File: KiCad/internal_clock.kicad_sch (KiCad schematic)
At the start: 8 parts, among them U1 TL074

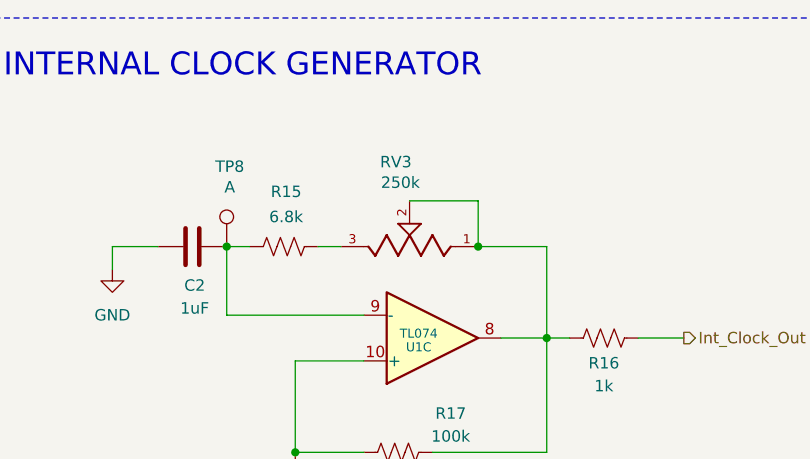
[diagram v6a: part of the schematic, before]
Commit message: re-placing components; optimizing text on silkscreen
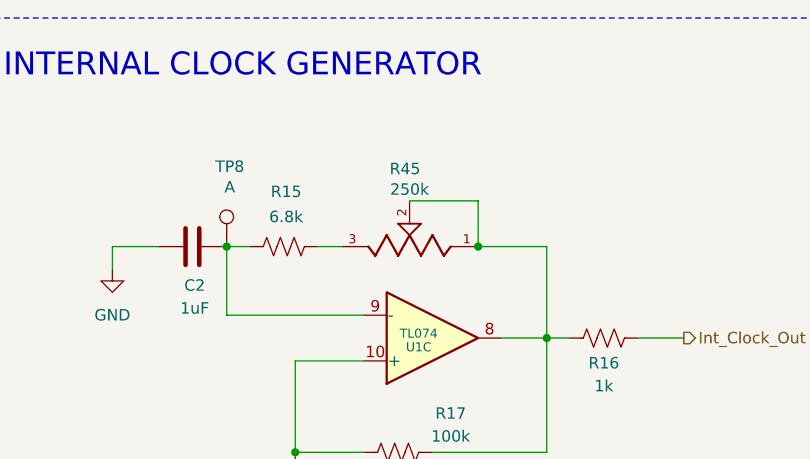
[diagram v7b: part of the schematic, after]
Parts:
- removed RV3: 250k, Eurorack:RD901F_1, symbol Eurorack:RD901F
- added R45: 250k, Eurorack:Potentiometer_Alpha_RD901F_Vertical_Alt, symbol Eurorack:Potentiometer_Alpha_RD901F_Vertical
- C2: footprint Eurorack:Kemet Film Cap -> Eurorack:Capacitor_Film_KEMET_R82DC4100AA60J_THT
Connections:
- net at R16.2, R17.1, U1.8: now also R45.1, R45.2
- net at R15.1: now also R45.3
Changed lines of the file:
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@@
-	)
-	(symbol
-		(lib_id "Eurorack:RD901F")
-		(at 68.58 45.72 180)
-		(unit 1)
-		(exclude_from_sim no)
-		(in_bom yes)
-		(on_board yes)
-		(dnp no)
-		(property "Reference" "RV3"
-			(at 67.056 36.322 0)
-			(effects
-				(font
-					(size 1.27 1.27)
-				)
-			)
-		)
-		(property "Value" "250k"
-			(at 67.564 38.608 0)
-			(effects
-				(font
-					(size 1.27 1.27)
-				)
-			)
-		)
-		(property "Footprint" "Eurorack:RD901F_1"
-			(at 68.58 45.72 0)
-			(effects
-				(font
-					(size 1.27 1.27)
-				)
-				(justify bottom)
-				(hide yes)
-			)
-		)
-		(property "Datasheet" ""
-			(at 68.58 45.72 0)
-			(effects
-				(font
-					(size 1.27 1.27)
-				)
-				(hide yes)
-			)
-		)
-		(property "Description" ""
-			(at 68.58 45.72 0)
-			(effects
-				(font
-					(size 1.27 1.27)
-				)
-				(hide yes)
-			)
-		)
-		(property "MF" ""
-			(at 68.58 45.72 0)
-			(effects
-				(font
-					(size 1.27 1.27)
-				)
-				(justify bottom)
-				(hide yes)
-			)
-		)
-		(property "MAXIMUM_PACKAGE_HEIGHT" ""
-			(at 68.58 45.72 0)
-			(effects
-				(font
-					(size 1.27 1.27)
-				)
-				(justify bottom)
-				(hide yes)
-			)
-		)
-		(property "Package" ""
-			(at 68.58 45.72 0)
-			(effects
-				(font
-					(size 1.27 1.27)
-				)
-				(justify bottom)
-				(hide yes)
-			)
-		)
-		(property "Price" ""
-			(at 68.58 45.72 0)
-			(effects
-				(font
-					(size 1.27 1.27)
-				)
-				(justify bottom)
-				(hide yes)
-			)
-		)
-		(property "Check_prices" ""
-			(at 68.58 45.72 0)
-			(effects
-				(font
-					(size 1.27 1.27)
-				)
-				(justify bottom)
-				(hide yes)
-			)
-		)
-		(property "STANDARD" ""
-			(at 68.58 45.72 0)
-			(effects
-				(font
-					(size 1.27 1.27)
-				)
-				(justify bottom)
-				(hide yes)
-			)
-		)
-		(property "PARTREV" ""
-			(at 68.58 45.72 0)
-			(effects
-				(font
-					(size 1.27 1.27)
-				)
-				(justify bottom)
-				(hide yes)
-			)
-		)
-		(property "SnapEDA_Link" ""
-			(at 68.58 45.72 0)
-			(effects
-				(font
-					(size 1.27 1.27)
-				)
-				(justify bottom)
-				(hide yes)
-			)
-		)
-		(property "MP" ""
-			(at 68.58 45.72 0)
-			(effects
-				(font
-					(size 1.27 1.27)
-				)
-				(justify bottom)
-				(hide yes)
-			)
-		)
-		(property "Description_1" ""
-			(at 68.58 45.72 0)
-			(effects
-				(font
-					(size 1.27 1.27)
-				)
-				(justify bottom)
-				(hide yes)
-			)
-		)
-		(property "Availability" ""
-			(at 68.58 45.72 0)
-			(effects
-				(font
-					(size 1.27 1.27)
-				)
-				(justify bottom)
-				(hide yes)
-			)
-		)
-		(property "MANUFACTURER" ""
-			(at 68.58 45.72 0)
-			(effects
-				(font
-					(size 1.27 1.27)
-				)
-				(justify bottom)
-				(hide yes)
-			)
-		)
-		(pin "1"
-		)
-		(pin "2"
-		)
-		(pin "3"
-		)
-		(instances
-			(project ""
-				(path "/c997e785-a132-463f-bd08-a5a67a697207/b964167f-08d9-430a-9aa0-9a2613885304"
-					(reference "RV3")
-					(unit 1)
-				)
-			)
-		)
 	)
 	(symbol
@@
 			)
 		)
-		(property "Footprint" "Eurorack:Kemet Film Cap"
+		(property "Footprint" "Eurorack:Capacitor_Film_KEMET_R82DC4100AA60J_THT"
 			(at 48.26 44.7548 0)
 			(effects
@@
 					(unit 1)
 				)
+			)
+		)
+	)
+	(symbol
+		(lib_id "Eurorack:Potentiometer_Alpha_RD901F_Vertical")
+		(at 68.58 45.72 180)
+		(unit 1)
+		(exclude_from_sim no)
+		(in_bom yes)
+		(on_board yes)
+		(dnp no)
+		(property "Reference" "R45"
+			(at 68.072 37.084 0)
+			(effects
+				(font
+					(size 1.27 1.27)
+				)
+			)
+		)
+		(property "Value" "250k"
+			(at 68.58 39.37 0)
+			(effects
+				(font
+					(size 1.27 1.27)
+				)
+			)
+		)
+		(property "Footprint" "Eurorack:Potentiometer_Alpha_RD901F_Vertical_Alt"
+			(at 68.58 45.72 0)
+			(effects
+				(font
+					(size 1.27 1.27)
+				)
+				(justify bottom)
+				(hide yes)
+			)
+		)
+		(property "Datasheet" ""
+			(at 68.58 45.72 0)
+			(effects
+				(font
+					(size 1.27 1.27)
+				)
+				(hide yes)
+			)
+		)
+		(property "Description" ""
+			(at 68.58 45.72 0)
+			(effects
+				(font
+					(size 1.27 1.27)
+				)
+				(hide yes)
+			)
+		)
+		(property "MF" ""
+			(at 68.58 45.72 0)
+			(effects
+				(font
+					(size 1.27 1.27)
+				)
+				(justify bottom)
+				(hide yes)
+			)
+		)
+		(property "MAXIMUM_PACKAGE_HEIGHT" ""
+			(at 68.58 45.72 0)
+			(effects
+				(font
+					(size 1.27 1.27)
+				)
+				(justify bottom)
+				(hide yes)
+			)
+		)
+		(property "Package" ""
+			(at 68.58 45.72 0)
+			(effects
+				(font
+					(size 1.27 1.27)
+				)
+				(justify bottom)
+				(hide yes)
+			)
+		)
+		(property "Price" ""
+			(at 68.58 45.72 0)
+			(effects
+				(font
+					(size 1.27 1.27)
+				)
+				(justify bottom)
+				(hide yes)
+			)
+		)
+		(property "Check_prices" ""
+			(at 68.58 45.72 0)
+			(effects
+				(font
+					(size 1.27 1.27)
+				)
+				(justify bottom)
+				(hide yes)
+			)
+		)
+		(property "STANDARD" ""
+			(at 68.58 45.72 0)
+			(effects
+				(font
+					(size 1.27 1.27)
+				)
+				(justify bottom)
+				(hide yes)
+			)
+		)
+		(property "PARTREV" ""
+			(at 68.58 45.72 0)
+			(effects
+				(font
+					(size 1.27 1.27)
+				)
+				(justify bottom)
+				(hide yes)
+			)
+		)
+		(property "SnapEDA_Link" ""
+			(at 68.58 45.72 0)
+			(effects
+				(font
+					(size 1.27 1.27)
+				)
+				(justify bottom)
+				(hide yes)
+			)
+		)
+		(property "MP" ""
+			(at 68.58 45.72 0)
+			(effects
+				(font
+					(size 1.27 1.27)
+				)
+				(justify bottom)
+				(hide yes)
+			)
+		)
+		(property "Description_1" ""
+			(at 68.58 45.72 0)
+			(effects
+				(font
+					(size 1.27 1.27)
+				)
+				(justify bottom)
+				(hide yes)
+			)
+		)
+		(property "Availability" ""
+			(at 68.58 45.72 0)
+			(effects
+				(font
+					(size 1.27 1.27)
+				)
+				(justify bottom)
+				(hide yes)
+			)
+		)
+		(property "MANUFACTURER" ""
+			(at 68.58 45.72 0)
+			(effects
+				(font
+					(size 1.27 1.27)
+				)
+				(justify bottom)
+				(hide yes)
+			)
+		)
+		(pin "1"
+		)
+		(pin "3"
+		)
+		(pin "2"
+		)
+		(instances
+			(project ""
+				(path "/c997e785-a132-463f-bd08-a5a67a697207/b964167f-08d9-430a-9aa0-9a2613885304"
+					(reference "R45")
+					(unit 1)
+				)

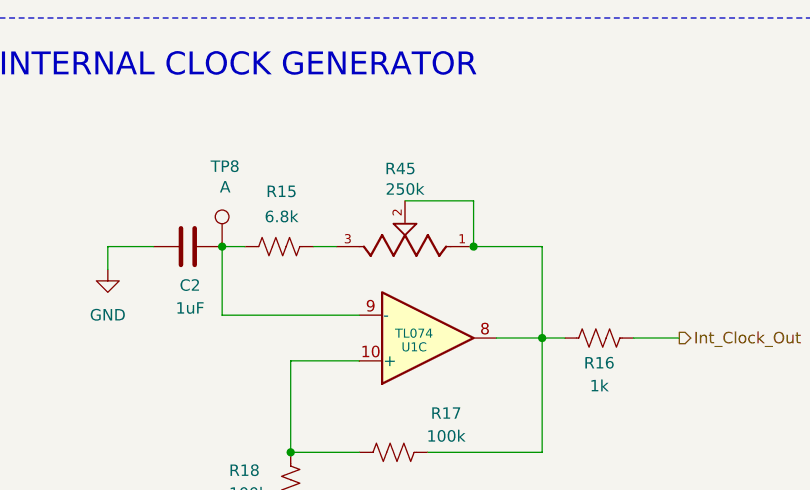
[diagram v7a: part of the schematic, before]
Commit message: fixing drc errors; mirroring potentiometers in sch due to error; mirroring switches on pcb
to do: change symbol description potentiometer (cw, ccw)
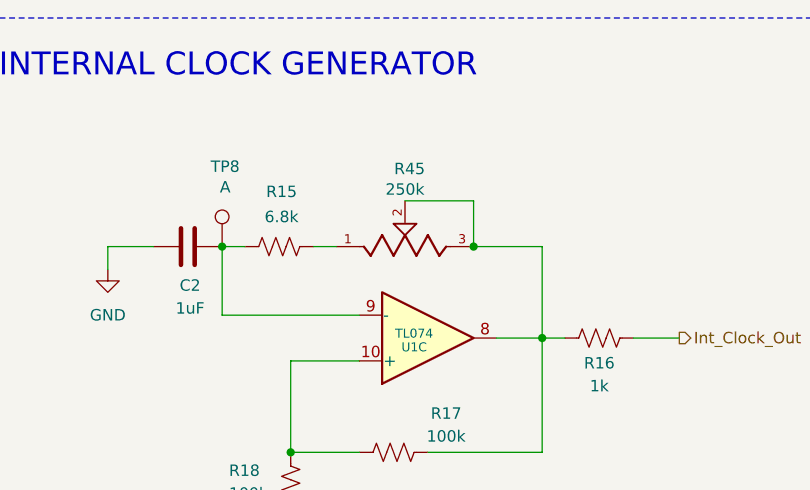
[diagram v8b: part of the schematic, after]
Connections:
- net at R16.2, R17.1, R45.2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: now also R45.3; no longer R45.1
- net at R15.1: now also R45.1; no longer R45.3
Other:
- moved on the sheet: R45
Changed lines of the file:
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@@
 	(symbol
 		(lib_id "Eurorack:Potentiometer_Alpha_RD901F_Vertical")
-		(at 68.58 45.72 180)
+		(at 68.58 45.72 0)
+		(mirror x)
 		(unit 1)
 		(exclude_from_sim no)
@@
 		(dnp no)
 		(property "Reference" "R45"
-			(at 68.072 37.084 0)
+			(at 69.088 37.084 0)
 			(effects
 				(font
